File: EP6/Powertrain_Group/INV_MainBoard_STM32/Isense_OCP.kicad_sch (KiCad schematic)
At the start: 28 parts, among them J11 current_U, J12 current_V, J13 current_W, J5 current_DC, J6 current_U, J7 current_V, J8 current_V

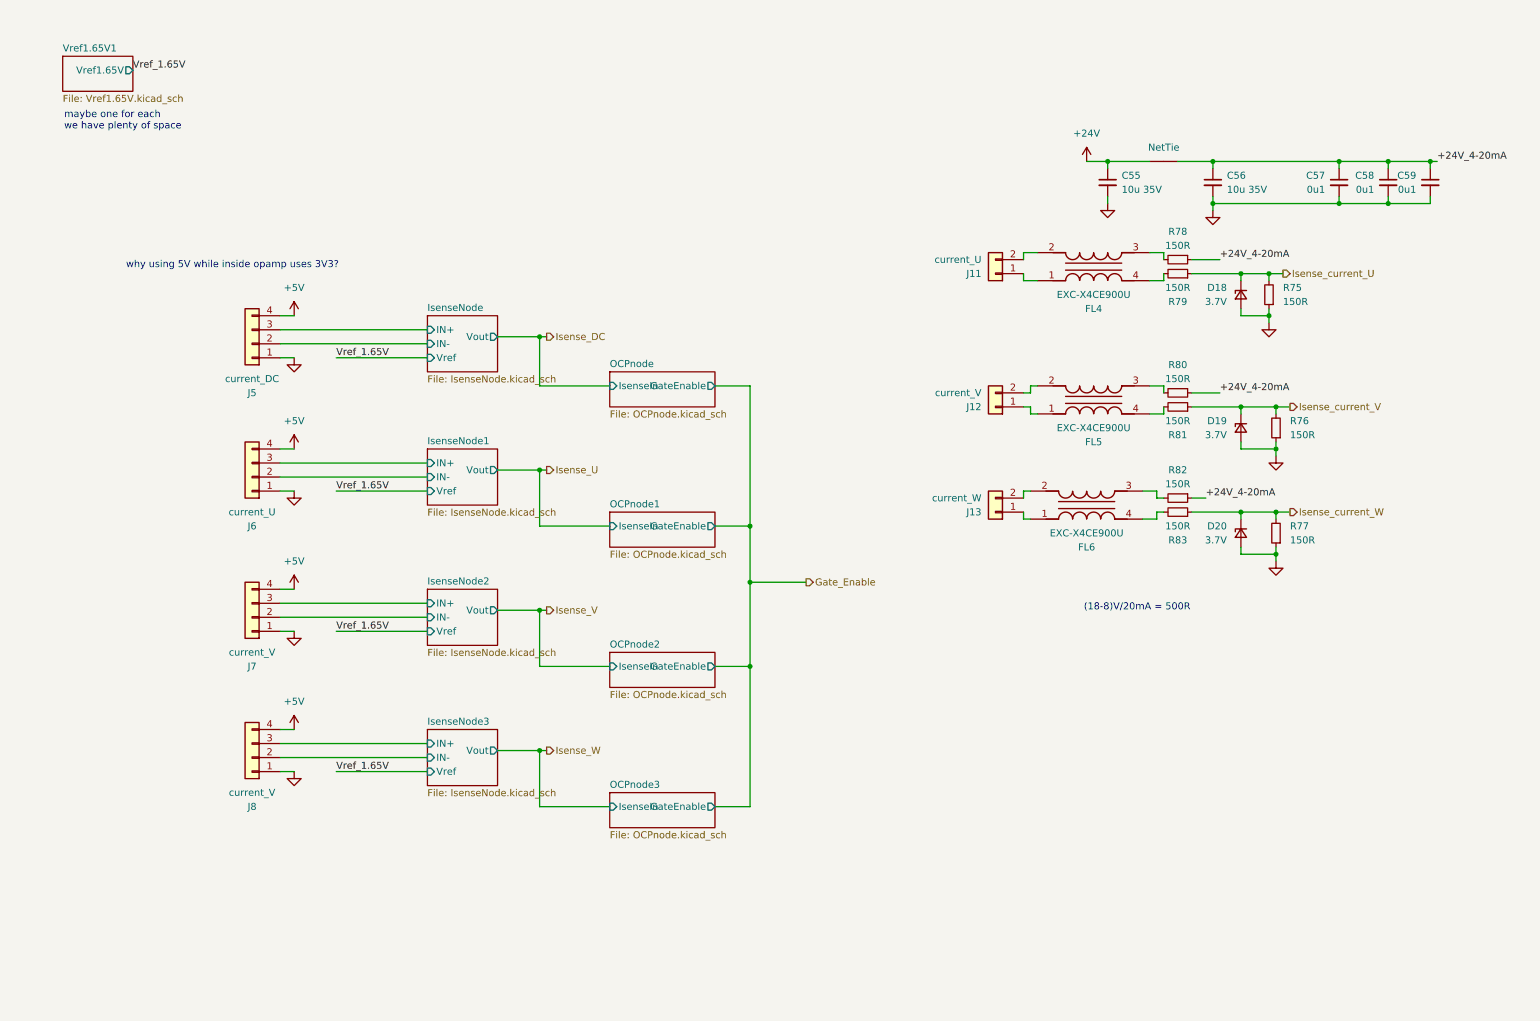
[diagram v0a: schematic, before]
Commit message: batch update for JLCPCB 241117
6SBMS
ACC_HVLV1
INV_CurrentSense2
INV_CurrentSense3
DClinkCap1
INV_MainBoard_STM32
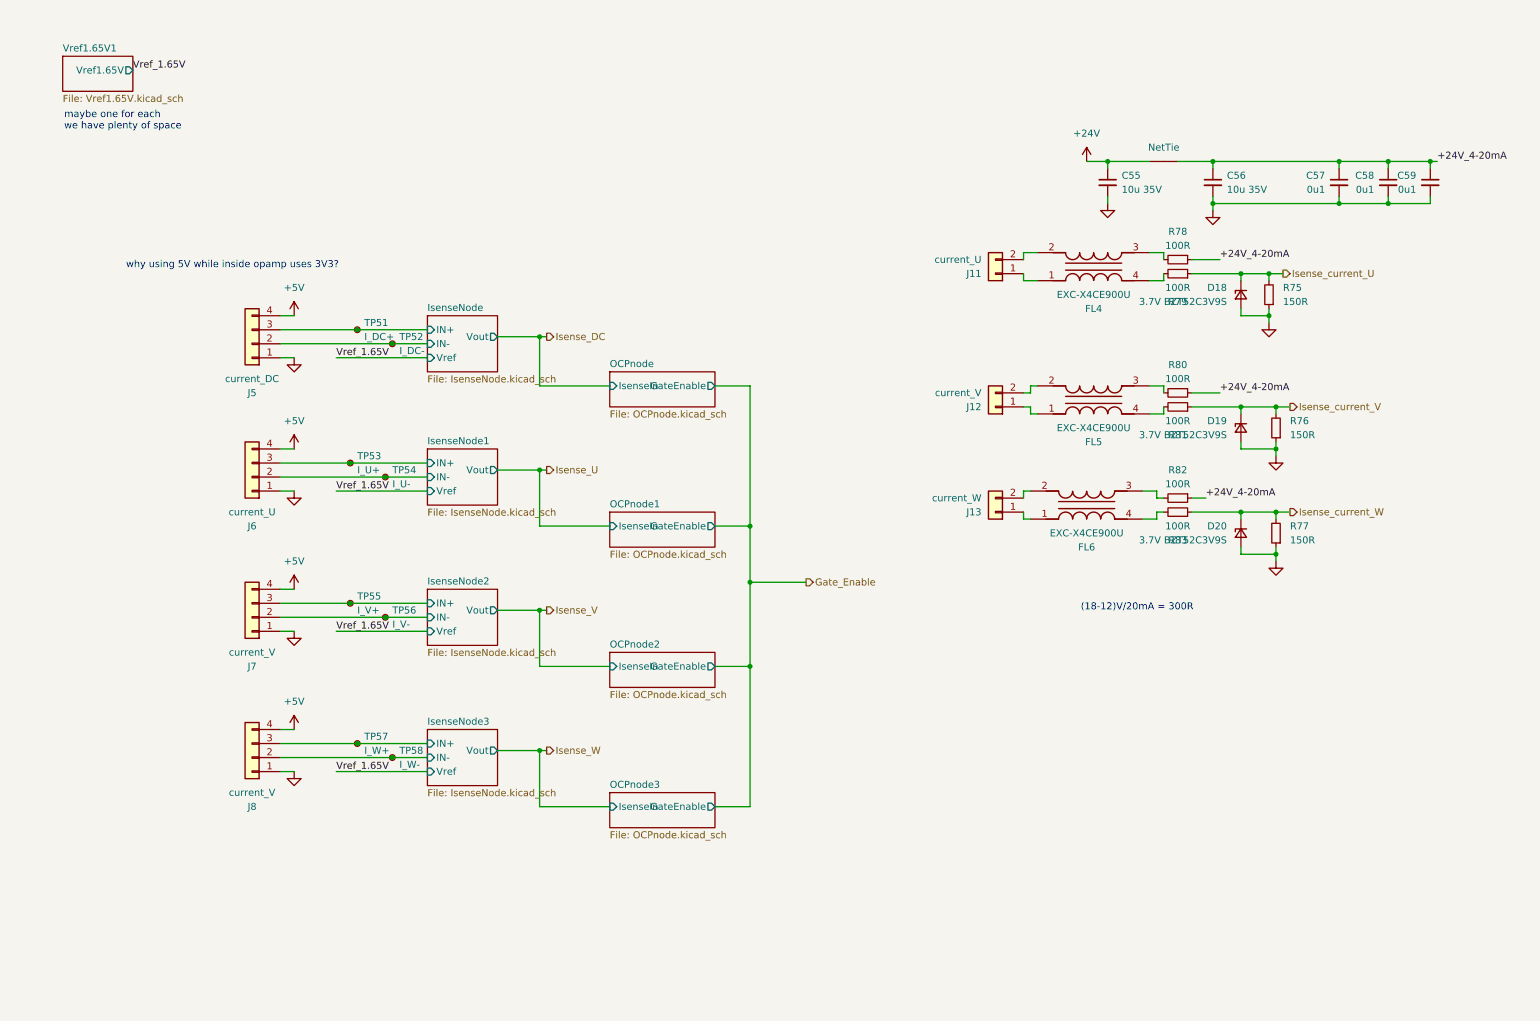
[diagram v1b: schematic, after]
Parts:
- added TP51: I_DC+, TestPoint:TestPoint_Pad_D1.0mm, symbol Connector:TestPoint_Small
- added TP52: I_DC-, TestPoint:TestPoint_Pad_D1.0mm, symbol Connector:TestPoint_Small
- added TP53: I_U+, TestPoint:TestPoint_Pad_D1.0mm, symbol Connector:TestPoint_Small
- added TP54: I_U-, TestPoint:TestPoint_Pad_D1.0mm, symbol Connector:TestPoint_Small
- added TP55: I_V+, TestPoint:TestPoint_Pad_D1.0mm, symbol Connector:TestPoint_Small
- added TP56: I_V-, TestPoint:TestPoint_Pad_D1.0mm, symbol Connector:TestPoint_Small
- added TP57: I_W+, TestPoint:TestPoint_Pad_D1.0mm, symbol Connector:TestPoint_Small
- added TP58: I_W-, TestPoint:TestPoint_Pad_D1.0mm, symbol Connector:TestPoint_Small
- D18, D19, D20: value 3.7V -> 3.7V BZT52C3V9S
- R75, R76, R77: footprint Resistor_SMD:R_0402_1005Metric -> Resistor_SMD:R_0603_1608Metric
- R78, R79, R80, R81, R82, R83: value 150R -> 100R; footprint Resistor_SMD:R_0402_1005Metric -> Resistor_SMD:R_0603_1608Metric
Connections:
- net IsenseNode/IN+: now also TP51.1
- net IsenseNode/IN-: now also TP52.1
- net IsenseNode1/IN+: now also TP53.1
- net IsenseNode1/IN-: now also TP54.1
- net IsenseNode2/IN+: now also TP55.1
- net IsenseNode2/IN-: now also TP56.1
- net IsenseNode3/IN+: now also TP57.1
- net IsenseNode3/IN-: now also TP58.1
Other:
- note added: "(18-12)V/20mA = 300R"
- note removed: "(18-8)V/20mA = 500R"

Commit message: update INV_MainBoard_STM32 to V2.0
big update to match new INV_GateDriver
and use H743ZI as MCU
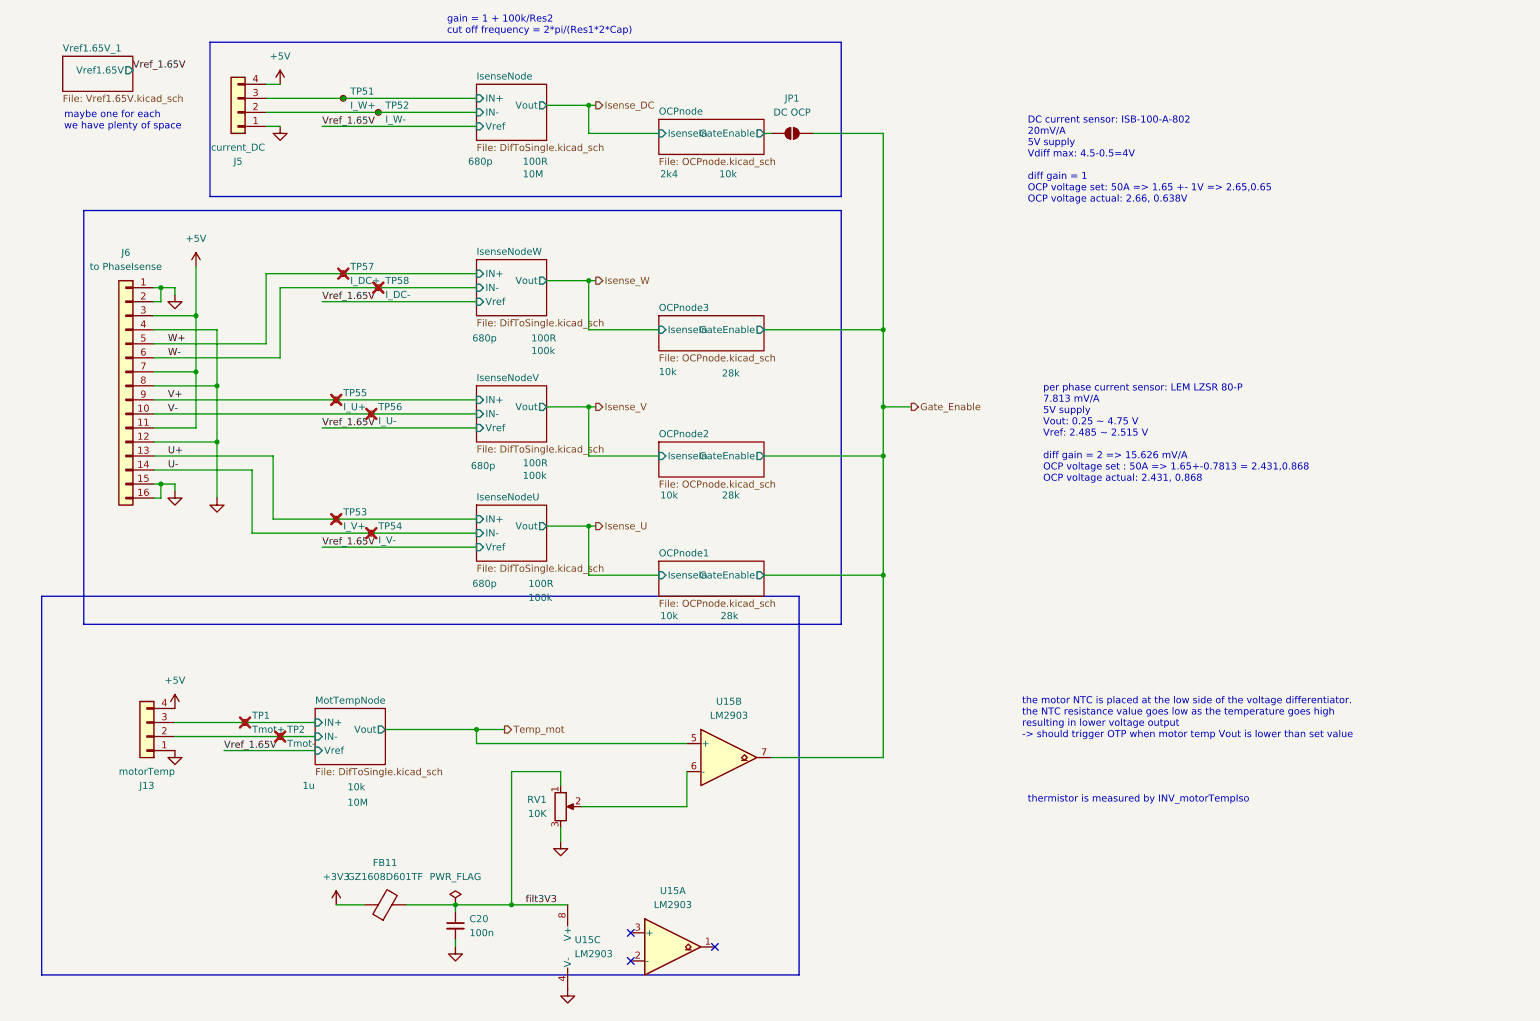
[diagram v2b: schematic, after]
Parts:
- removed C55, C56: 10u 35V, Capacitor_SMD:C_1206_3216Metric, symbol Device:C_Small
- removed C57, C58, C59: 0u1, Capacitor_SMD:C_0402_1005Metric, symbol Device:C_Small
- removed D18, D19, D20: 3.7V BZT52C3V9S, Diode_SMD:D_SOD-323, symbol Device:D_Zener_Small
- removed FL4, FL5, FL6: EXC-X4CE900U, SamacSys_Parts_EP6:EXCX4CE900U, symbol SamacSys_Parts_EP6:EXC-X4CE900U
- removed J11: current_U, Connector_JST:JST_XH_B2B-XH-A_1x02_P2.50mm_Vertical, symbol Connector_Generic:Conn_01x02
- removed J12: current_V, Connector_JST:JST_XH_B2B-XH-A_1x02_P2.50mm_Vertical, symbol Connector_Generic:Conn_01x02
- removed J13: current_W, Connector_JST:JST_XH_B2B-XH-A_1x02_P2.50mm_Vertical, symbol Connector_Generic:Conn_01x02
- removed J6: current_U, Connector_JST:JST_XH_B4B-XH-A_1x04_P2.50mm_Vertical, symbol PCM_4ms_Connector:Conn_01x04
- removed J7, J8: current_V, Connector_JST:JST_XH_B4B-XH-A_1x04_P2.50mm_Vertical, symbol PCM_4ms_Connector:Conn_01x04
- removed R75, R76, R77: 150R, Resistor_SMD:R_0603_1608Metric, symbol Device:R_Small
- removed R78, R79, R80, R81, R82, R83: 100R, Resistor_SMD:R_0603_1608Metric, symbol Device:R_Small
- removed TIE1: NetTie, NetTie:NetTie-2_SMD_Pad0.5mm, symbol PCM_4ms_Net-tie:NetTie
- added C20: 100n, Capacitor_SMD:C_0402_1005Metric, symbol Device:C_Small
- added FB11: GZ1608D601TF, Capacitor_SMD:C_0603_1608Metric, symbol Device:FerriteBead
- added J13: motorTemp, Connector_JST:JST_XH_B4B-XH-A_1x04_P2.50mm_Vertical, symbol Connector_Generic:Conn_01x04
- added J6: to PhaseIsense, Connector_PinHeader_2.54mm:PinHeader_1x16_P2.54mm_Horizontal, symbol Connector_Generic:Conn_01x16
- added JP1: DC OCP, Jumper:SolderJumper-2_P1.3mm_Open_RoundedPad1.0x1.5mm, symbol Jumper:SolderJumper_2_Open
- added RV1: 10K, nturt_kicad_lib_EP6:Throughhole Potentiometer 3296W, symbol Device:R_Potentiometer
- added TP1: Tmot+, TestPoint:TestPoint_Pad_D1.0mm, symbol Connector:TestPoint_Small
- added TP2: Tmot-, TestPoint:TestPoint_Pad_D1.0mm, symbol Connector:TestPoint_Small
- added U15: LM2903, Package_SO:SOIC-8_3.9x4.9mm_P1.27mm, symbol Comparator:LM2903
- TP51: value I_DC+ -> I_W+
- TP52: value I_DC- -> I_W-
- TP53: value I_U+ -> I_V+; now not fitted; now left out of the parts list
- TP54: value I_U- -> I_V-; now not fitted; now left out of the parts list
- TP55: value I_V+ -> I_U+; now not fitted; now left out of the parts list
- TP56: value I_V- -> I_U-; now not fitted; now left out of the parts list
- TP57: value I_W+ -> I_DC+; now not fitted; now left out of the parts list
- TP58: value I_W- -> I_DC-; now not fitted; now left out of the parts list
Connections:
- net +5V: now also J13.4 (Pin_4), J6.11 (Pin_11), J6.3 (Pin_3), J6.7 (Pin_7)
- net GND: now also C20.2, J13.1 (Pin_1), J6.1 (Pin_1), J6.12 (Pin_12), J6.15 (Pin_15), J6.16 (Pin_16), J6.2 (Pin_2), J6.4 (Pin_4), J6.8 (Pin_8), RV1.3, U15.4 (V-)
- net Gate_Enable: now also JP1.2 (B), U15.7
- net IsenseNodeU/IN+ renamed U+
- net U+: now also J6.13 (Pin_13)
- net IsenseNodeU/IN- renamed U-
- net U-: now also J6.14 (Pin_14)
- net IsenseNodeV/IN+ renamed V+
- net V+: now also J6.9 (Pin_9)
- net IsenseNodeV/IN- renamed V-
- net V-: now also J6.10 (Pin_10)
- net IsenseNodeW/IN+ renamed W+
- net W+: now also J6.5 (Pin_5)
- net IsenseNodeW/IN- renamed W-
- net W-: now also J6.6 (Pin_6)
- new net: RV1.2, U15.6 (-)
- new net +3V3: FB11.1
- new net MotTempNode/IN+: J13.3 (Pin_3), TP1.1
- new net MotTempNode/IN-: J13.2 (Pin_2), TP2.1
- new net OCPnode/GateEnable: JP1.1 (A)
- new net Temp_mot: U15.5 (+)
- new net filt3V3: C20.1, FB11.2, RV1.1, U15.8 (V+)
- no-connect marks 0 -> 3
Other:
- sheet IsenseNode1 renamed IsenseNodeU
- sheet IsenseNode2 renamed IsenseNodeV
- sheet IsenseNode3 renamed IsenseNodeW
- sheet Vref1.65V1 renamed Vref1.65V_1
- added sheet MotTempNode (DifToSingle.kicad_sch)
- sheet IsenseNode: file IsenseNode.kicad_sch -> DifToSingle.kicad_sch
- sheet IsenseNodeU: file IsenseNode.kicad_sch -> DifToSingle.kicad_sch
- sheet IsenseNodeV: file IsenseNode.kicad_sch -> DifToSingle.kicad_sch
- sheet IsenseNodeW: file IsenseNode.kicad_sch -> DifToSingle.kicad_sch
- note added: "DC current sensor: ISB-100-A-802 20mV/A 5V supply Vdiff max: 4.5-0.5=4V diff gain = 1 OCP voltage set: 50A => 1.65 +- 1V => 2.65,0.65 OCP voltage actual: 2.66, 0.638V"
- note added: "gain = 1 + 100k/Res2 cut off frequency = 2*pi/(Res1*2*Cap)"
- note added: "per phase current sensor: LEM LZSR 80-P 7.813 mV/A 5V supply Vout: 0.25 ~ 4.75 V Vref: 2.485 ~ 2.515 V diff gain = 2 => 15.626 mV/A OCP voltage set : 50A => 1.65+-0.7813 = 2.431,0.868 OCP voltage actual: 2.431, 0.868"
- note added: "the motor NTC is placed at the low side of the voltage differentiator. the NTC resistance value goes low as the temperature goes high resulting in lower voltage output -> should trigger OTP when motor temp Vout is lower than set value"
- note added: "thermistor is measured by INV_motorTempIso"
- note removed: "(18-12)V/20mA = 300R"
- note removed: "why using 5V while inside opamp uses 3V3?"
- title: INV_MainBoard -> INV_MainBoard_STM32
- moved on the sheet: J5, TP51, TP52
